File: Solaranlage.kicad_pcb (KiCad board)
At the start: 2 copper layers, 160 x 85 mm, 79 parts, among them J1 Screw_Terminal_01x02, J10 Conn_01x01_Male, J2 Screw_Terminal_01x02, J3 AVR-JTAG-10, J4 USB_B, J5 USB_B, J6 Screw_Terminal_01x02, J7 Conn_01x02_Male, J8 Conn_01x01_Male, J9 Conn_01x02_Male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

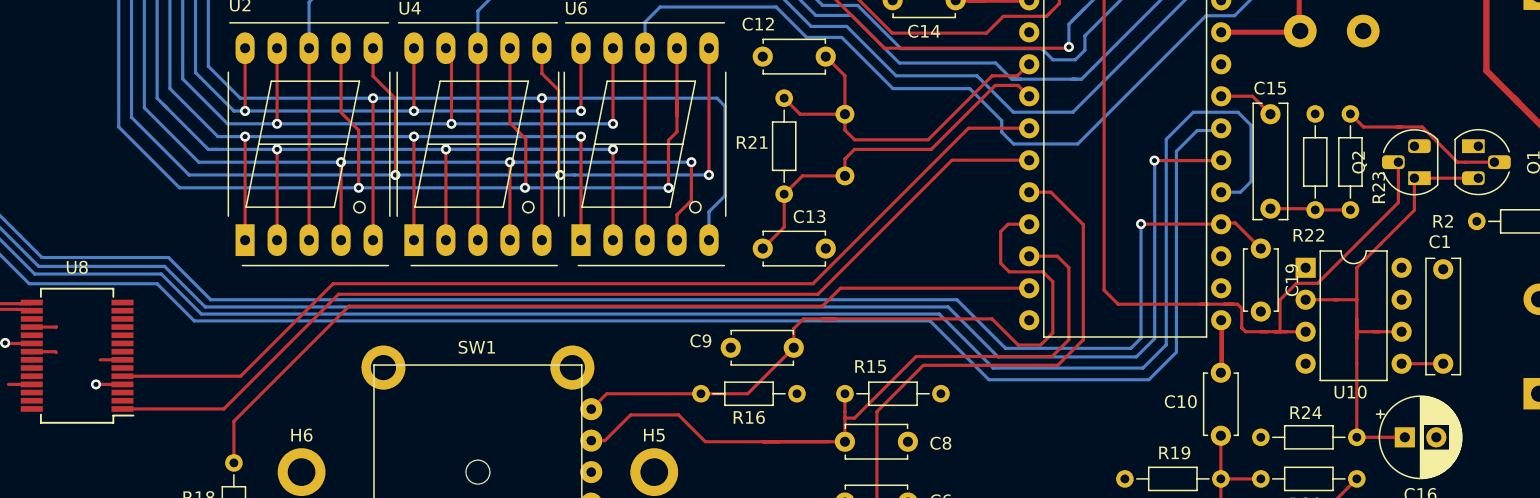
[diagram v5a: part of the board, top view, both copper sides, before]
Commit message: added simualtion for analog amp; applied changes in footprints
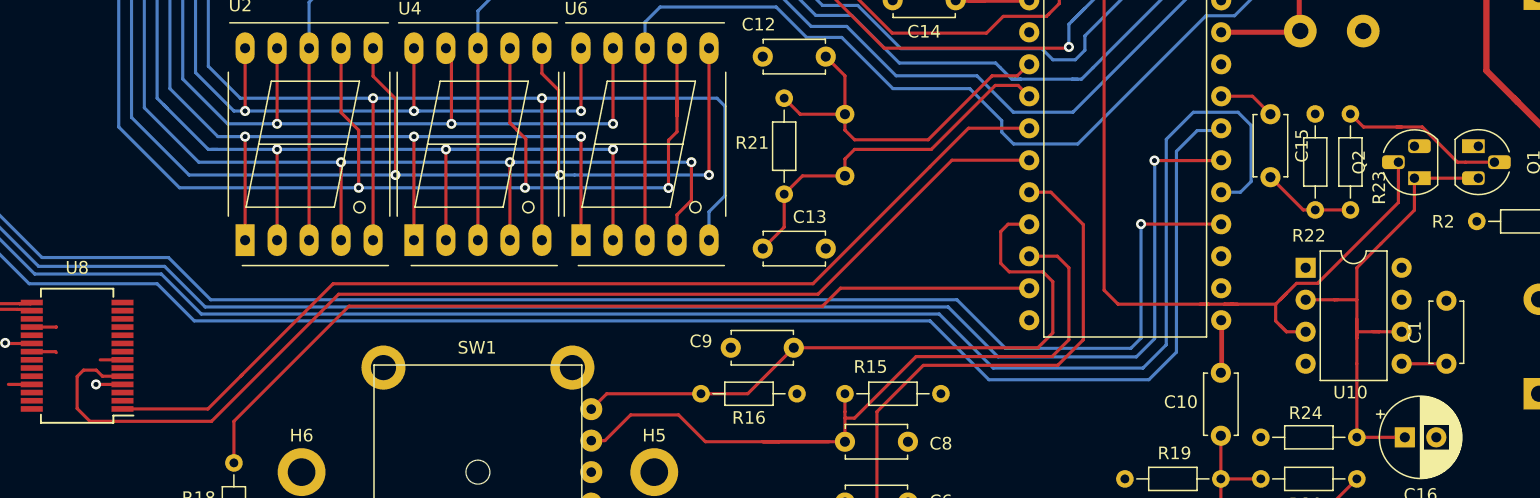
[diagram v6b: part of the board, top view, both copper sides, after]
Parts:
- removed C19: 10p, Capacitor_THT:C_Disc_D4.7mm_W2.5mm_P5.00mm
- C1, C15: footprint Capacitor_THT:C_Rect_L9.0mm_W2.5mm_P7.50mm_MKT -> Capacitor_THT:C_Disc_D4.7mm_W2.5mm_P5.00mm
- moved C1 0.25 mm to (215.9, 114.8)
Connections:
- U2 pad 3: /DZ -> /KH
- U2 pad 8: /DZ -> /KH
- U3 pad 3: /DE -> /DZ
- U3 pad 8: /DE -> /DZ
- U4 pad 3: /KH -> /KZ
- U4 pad 8: /KH -> /KZ
- U5 pad 3: /KZ -> /DE
- U5 pad 8: /KZ -> /DE
- U7 pad 34: /DZ -> /KH
- U7 pad 35: /DE -> /DZ
- U7 pad 36: /KH -> /KZ
- U7 pad 37: /KZ -> /DE
- U8 pad 1: TxD -> RxD
- U8 pad 5: RxD -> TxD
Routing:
- net /KZ: track 76.3 -> 101.1 mm, vias 2 -> 0
- net /DZ: track 106.9 -> 88.8 mm, vias 0 -> 2
- net /DE: track 88.8 -> 76.3 mm
- net TxD: track 80.1 -> 90.7 mm
- net /KH: track 101.1 -> 106.9 mm
- net TCK: track 162.3 -> 158.4 mm
- net SW1: track 56.6 -> 53.0 mm
- net \RST: track 218.6 -> 216.7 mm
- net RxD: track 80.1 -> 81.3 mm
- net Net-(C15-Pad2): track 6.39 -> 7.57 mm

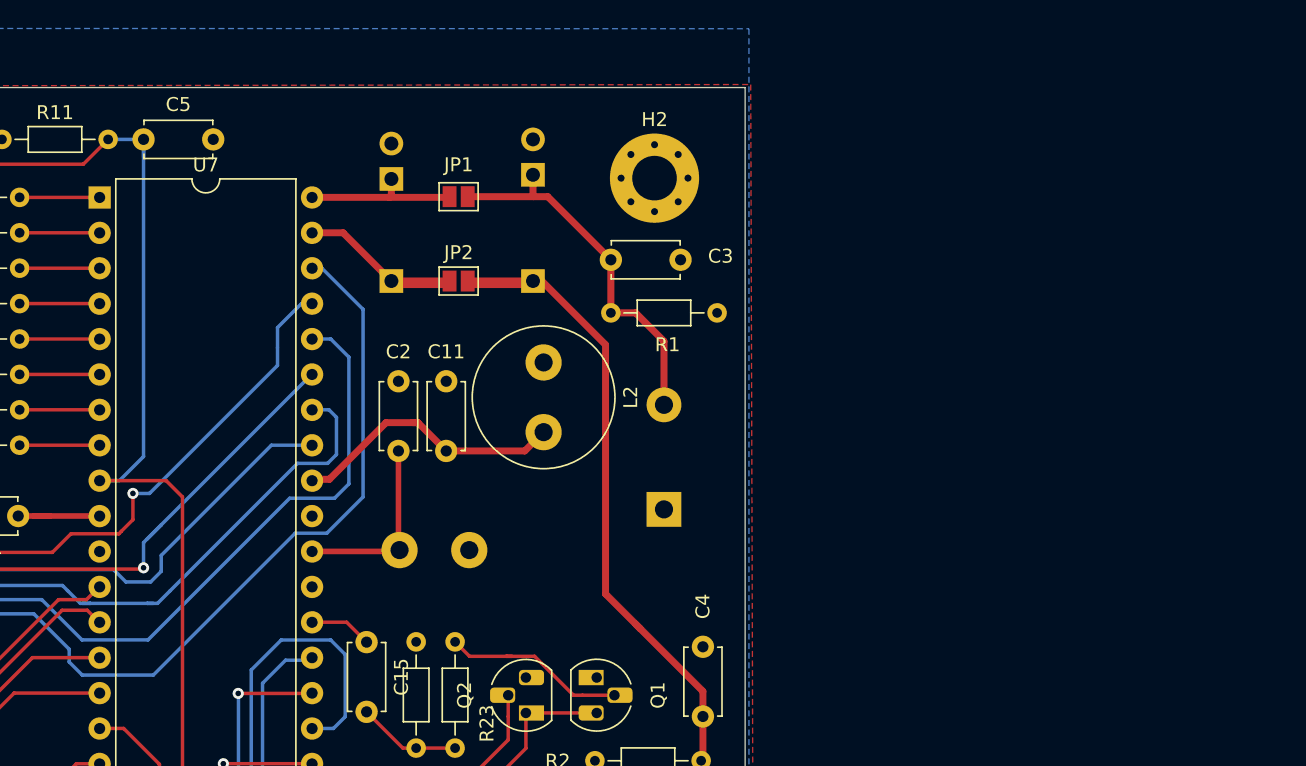
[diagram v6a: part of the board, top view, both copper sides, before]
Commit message: added amps for measureing
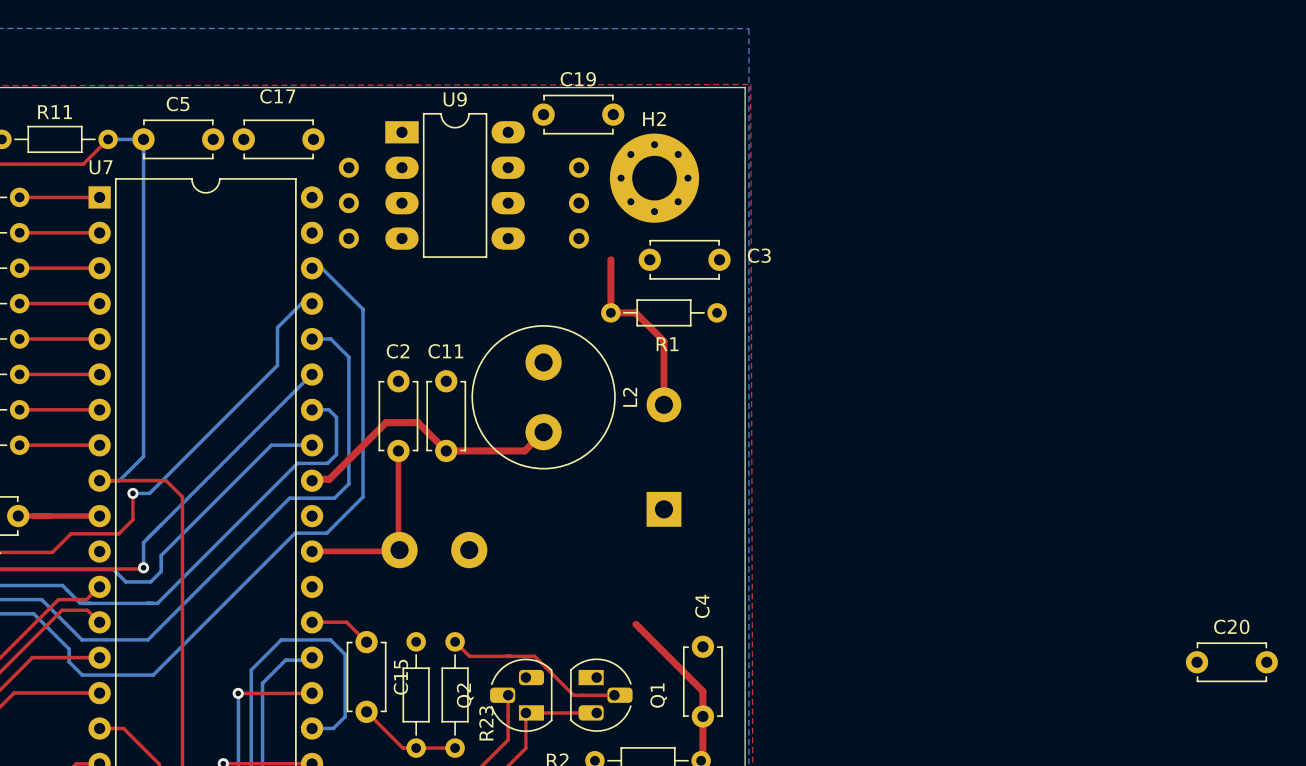
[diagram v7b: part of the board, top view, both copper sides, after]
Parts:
- removed J10, J8: Conn_01x01_Male, Connector_PinHeader_2.54mm:PinHeader_1x01_P2.54mm_Vertical
- removed J7, J9: Conn_01x02_Male, Connector_PinHeader_2.54mm:PinHeader_1x02_P2.54mm_Vertical
- removed JP1, JP2: Jumper, Jumper:SolderJumper-2_P1.3mm_Open_Pad1.0x1.5mm
- added C17: 10n, Capacitor_THT:C_Disc_D4.7mm_W2.5mm_P5.00mm, F.Cu at (198.1, 58.9)
- added C19: 10n, Capacitor_THT:C_Disc_D4.7mm_W2.5mm_P5.00mm, F.Cu at (214.6, 57.1)
- added C20: 10n, Capacitor_THT:C_Disc_D4.7mm_W2.5mm_P5.00mm, F.Cu at (261.5, 96.4)
- added RV1: R_POT_TRIM, Potentiometer_THT:Potentiometer_Bourns_3299W_Vertical, B.Cu at (200.7, 61.0)
- added RV2: R_POT_TRIM, Potentiometer_THT:Potentiometer_Bourns_3299W_Vertical, B.Cu at (217.2, 61.0)
- added U9: TS912, Package_DIP:DIP-8_W7.62mm_LongPads, F.Cu at (204.5, 58.4)
- moved C3 2.79 mm to (222.2, 67.6)
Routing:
- net Net-(C4-Pad1): track 56.7 -> 19.1 mm
- net /KELLER_ADC: track 16.2 -> 0.48 mm
- net Net-(C3-Pad1): track 26.8 -> 13.0 mm
- net /DACH_ADC: track 11.3 -> 0.00 mm

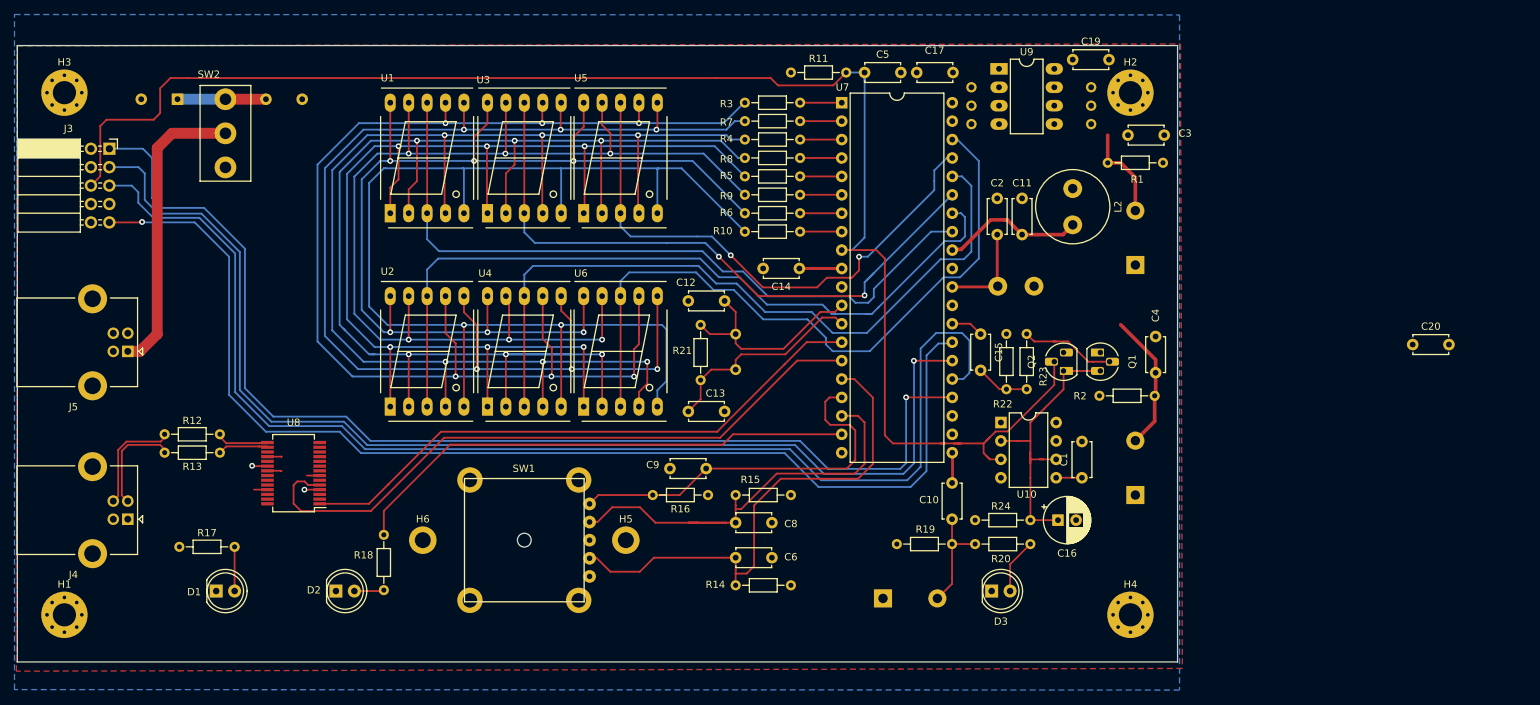
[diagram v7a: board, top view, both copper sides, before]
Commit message: applied changes to layout; added keepouts to supply of MCU and OP; DRC no issues
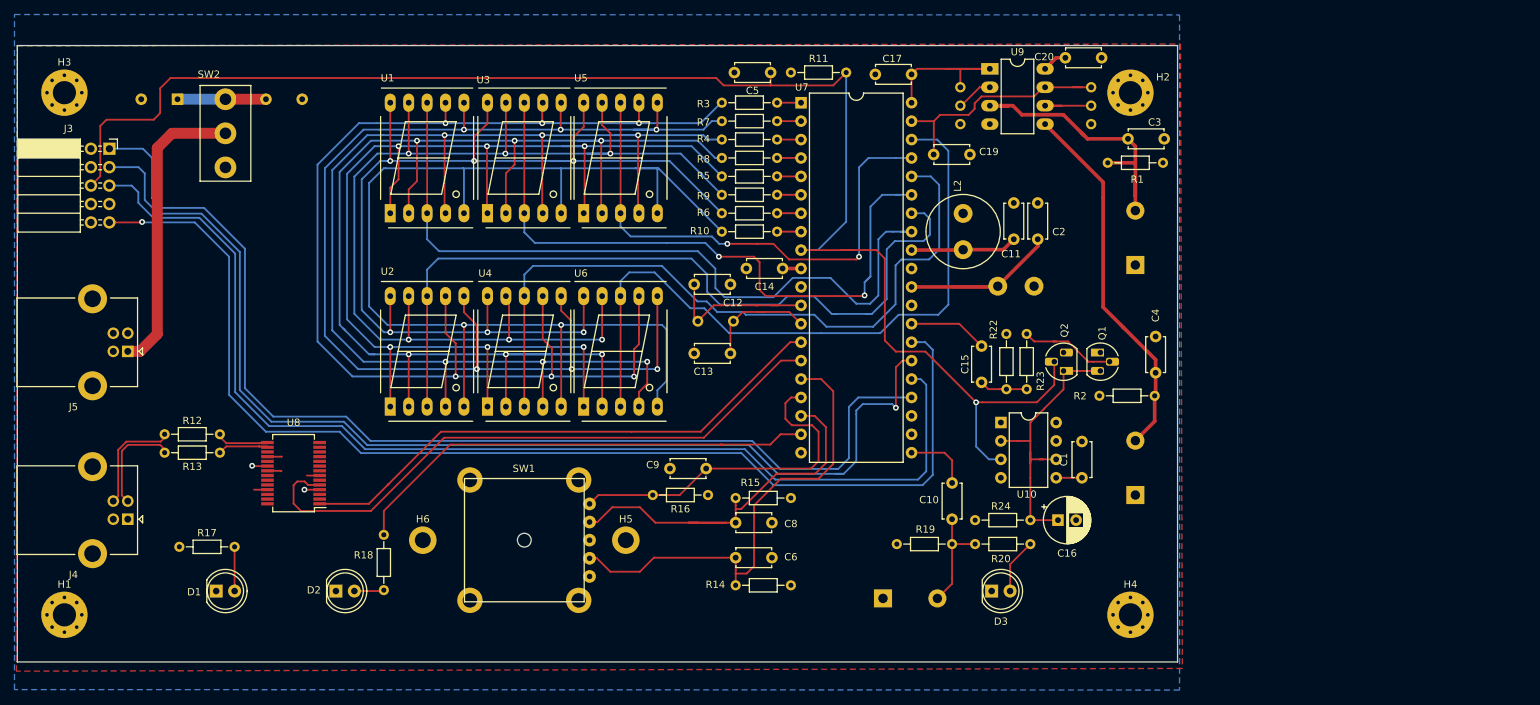
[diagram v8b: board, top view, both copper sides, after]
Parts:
- removed R21: 1Meg, Resistor_THT:R_Axial_DIN0204_L3.6mm_D1.6mm_P7.62mm_Horizontal
- moved C20 62.1 mm to (213.6, 56.9)
- moved C19 23.2 mm to (195.5, 70.2)
- moved L2 15.5 mm to (199.5, 78.4)
- moved C5 13.0 mm to (173.0, 58.9), turned to 180 degrees
- moved C13 9.89 mm to (167.4, 97.7), turned to 180 degrees
- moved C17 5.72 mm to (192.4, 59.2)
- moved C2 5.62 mm to (209.8, 81.9)
- moved U7 5.61 mm to (177.2, 63.1)
- moved Y1 5.50 mm to (162.9, 93.2), turned to 0 degrees
- moved C12 4.77 mm to (162.4, 88.1), turned to 0 degrees
- moved R10 3.18 mm to (173.9, 80.9)
- moved R3 3.18 mm to (173.9, 63.1)
- moved R4 3.18 mm to (173.9, 68.2)
- moved R5 3.18 mm to (173.9, 73.2)
- moved R6 3.18 mm to (173.9, 78.3)
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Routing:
- net Net-(C4-Pad1): track 19.1 -> 51.8 mm
- net /KELLER_ADC: track 0.48 -> 33.1 mm
- net Net-(C3-Pad1): track 13.0 -> 39.4 mm
- net /DACH_ADC: track 0.00 -> 23.7 mm
- net TMS: track 173.1 -> 156.3 mm
- net /AVCC: track 13.4 -> 27.0 mm
- net /XTAL1: track 29.2 -> 16.2 mm
- net /XTAL2: track 29.2 -> 21.8 mm
- net Net-(RV2-Pad2): track 0.00 -> 7.37 mm
- net TCK: track 158.4 -> 151.5 mm, vias 1 -> 0
- net WDI: track 4.53 -> 10.9 mm
- net RxD: track 81.3 -> 75.8 mm
- net TxD: track 90.7 -> 85.1 mm
- net ENC_B: track 61.8 -> 56.3 mm
- net TDO: track 161.8 -> 156.5 mm
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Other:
- rule trace_min: 0.1 -> 0
